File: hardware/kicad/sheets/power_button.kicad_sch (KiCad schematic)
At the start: 22 parts, among them J7 PANEL BUTTON, Q1 IRF4905S, Q2 BSS138, Q3 BSS138, Q4 BSS138, SW3 POWER, U11 LTC2954CTS8-2, U12 LM4040DBZ-5, U13 CL25N8-G

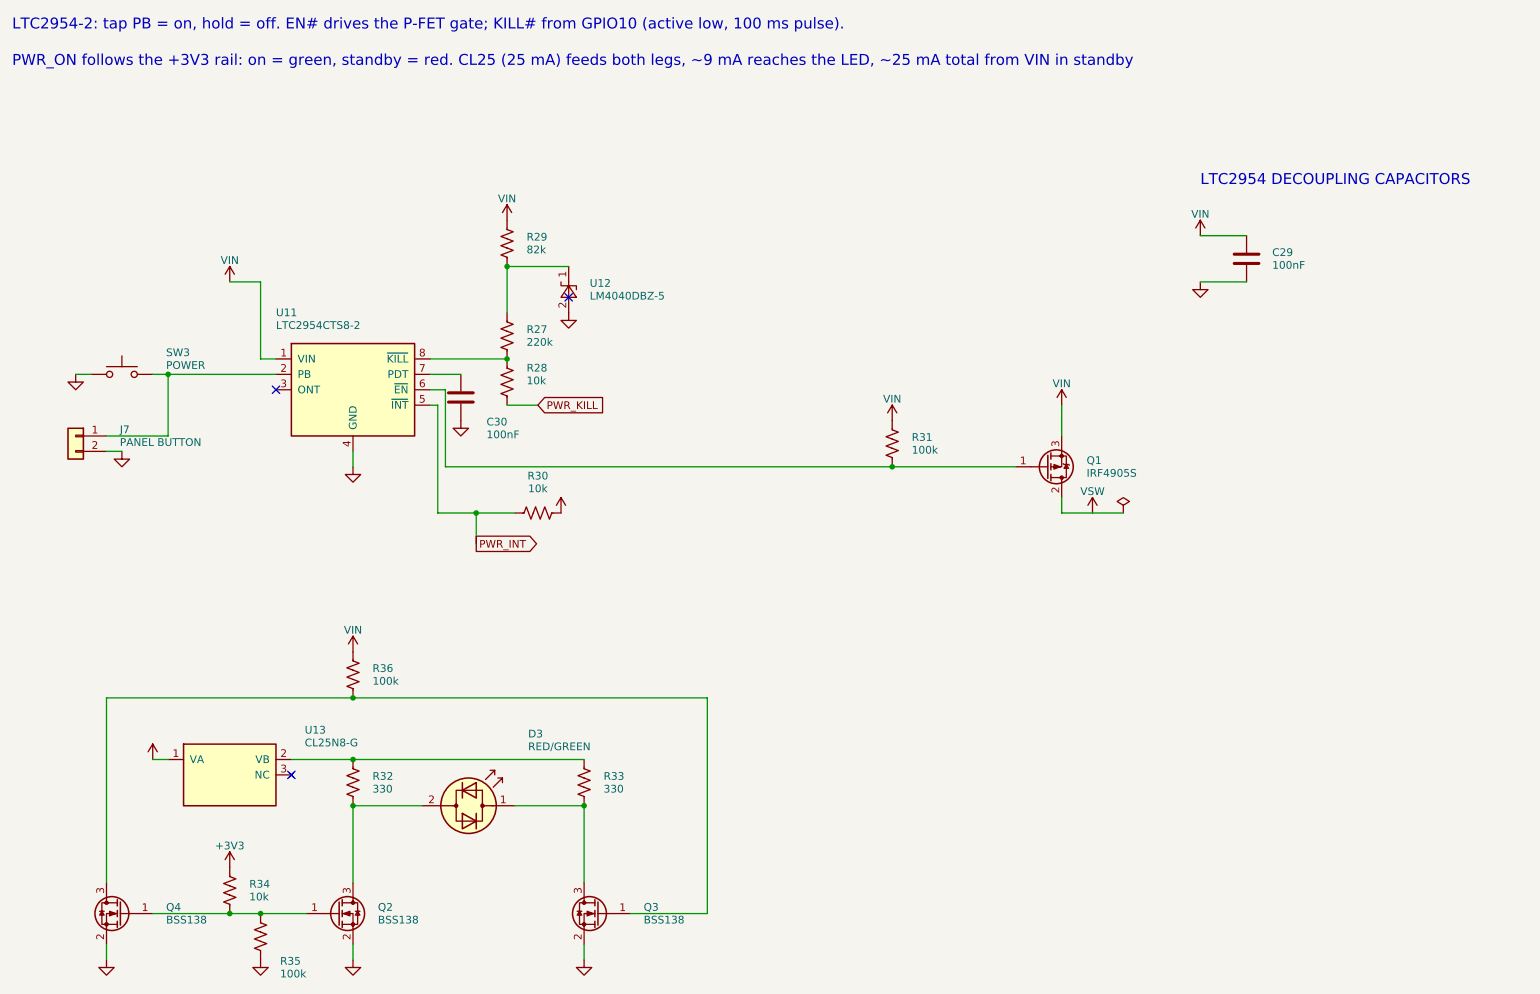
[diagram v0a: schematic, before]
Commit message: Put supply pins on top and grounds on the bottom of IC symbols; flake8-clean Python
Schematic: re-laid out pins on U2, U3, U6, U7, U11, U14, U17-U20, U22-U24
and PS1 (supply on top, ground/strap pins on the bottom edge) via custom
`cryocooler:` symbols (make_lib.from_stock) and a gnd_bus helper; U18/U2
use mirroring instead of a 180 degree rotation. Nets are unchanged (ERC 0,
117/117 datasheet rules, PCB nets still match). Text placement now shows
every power-symbol name, avoids wires, and uses a realistic character width.

Python: black -l 79 -S plus manual wrapping so hardware/kicad and scripts/
pass flake8; add .flake8.

Co-Authored-By: Claude Sonnet 5.5 <noreply@anthropic.com>
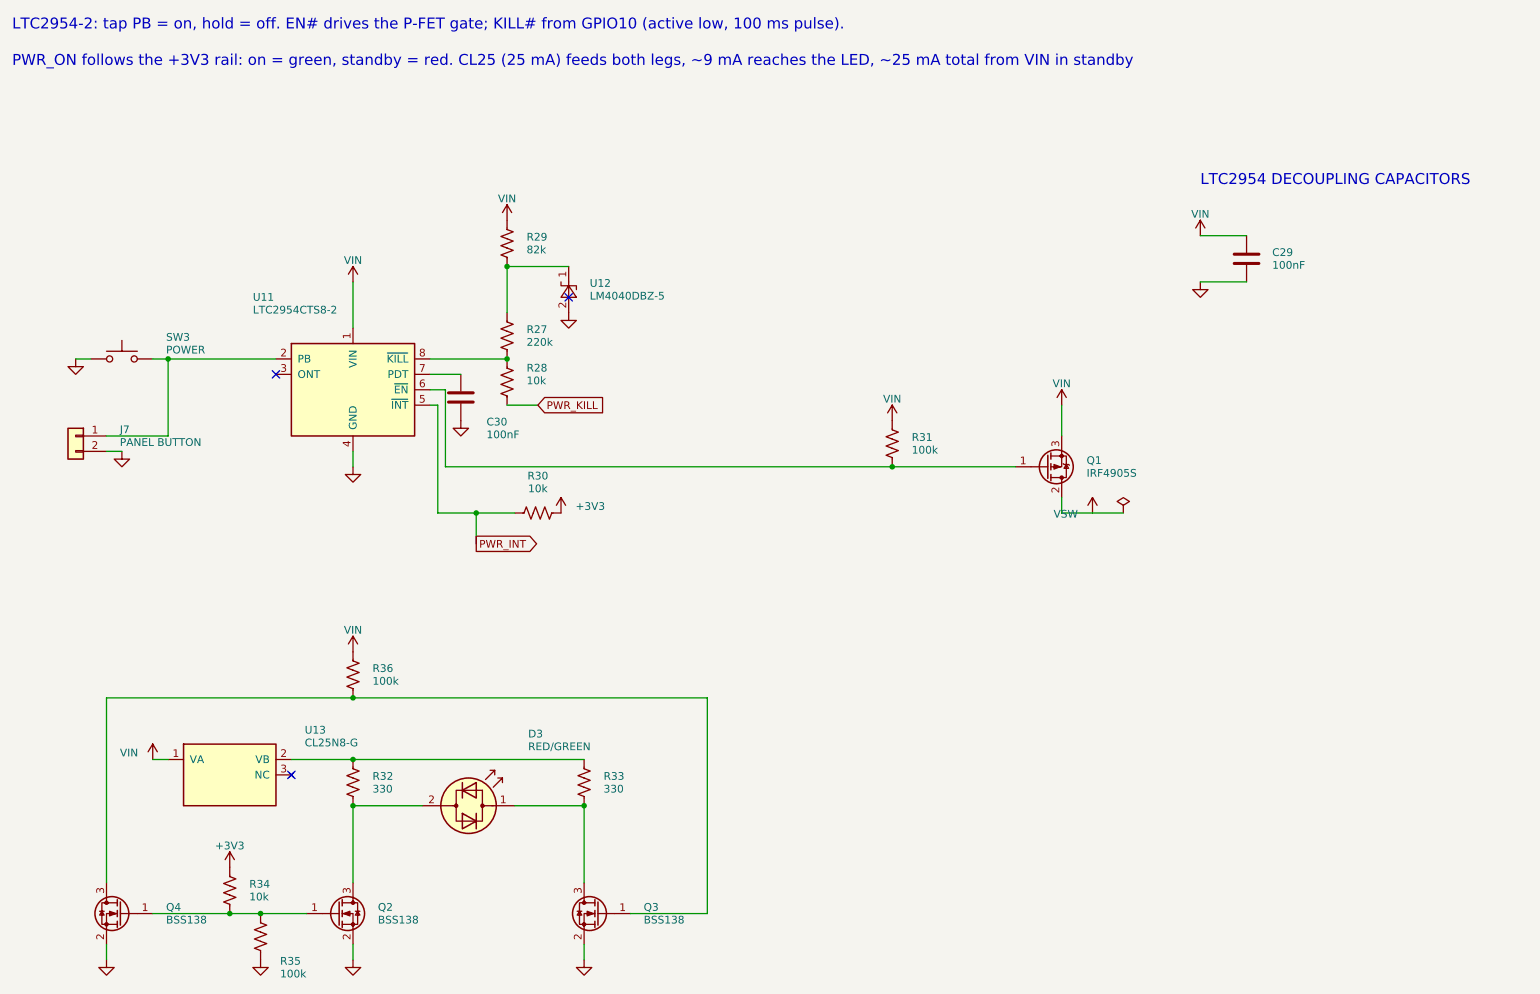
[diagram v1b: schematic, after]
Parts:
- removed D3: RED/GREEN, LED_SMD:LED_1206_3216Metric, symbol Device:LED_Dual_Bidirectional
- removed Q1: IRF4905S, Package_TO_SOT_SMD:TO-263-3_TabPin2, symbol Transistor_FET:IRF4905
- removed R36: 100k, Resistor_SMD:R_0603_1608Metric, symbol Device:R_US
- added C29: 100nF, Capacitor_SMD:C_0603_1608Metric, symbol Device:C
- added R33: 330, Resistor_SMD:R_0603_1608Metric, symbol Device:R_US
- added U13: CL25N8-G, Package_TO_SOT_SMD:SOT-89-3, symbol cryocooler:CL25N8-G
- C30: renamed from U12; value LM4040DBZ-5 -> 100nF; footprint Package_TO_SOT_SMD:SOT-23 -> Capacitor_SMD:C_0603_1608Metric; symbol Reference_Voltage:LM4040DBZ-5 -> Device:C
- D3: renamed from R32; value 330 -> RED/GREEN; footprint Resistor_SMD:R_0603_1608Metric -> LED_SMD:LED_1206_3216Metric; symbol Device:R_US -> Device:LED_Dual_Bidirectional
- J7: renamed from SW3; value POWER -> PANEL BUTTON; footprint Button_Switch_SMD:SW_SPST_TL3342 -> Connector_JST:JST_XH_B2B-XH-A_1x02_P2.50mm_Vertical; symbol Switch:SW_Push -> Connector_Generic:Conn_01x02
- Q1: renamed from R30; value 10k -> IRF4905S; footprint Resistor_SMD:R_0603_1608Metric -> Package_TO_SOT_SMD:TO-263-3_TabPin2; symbol Device:R_US -> Transistor_FET:IRF4905
- Q2: renamed from R33; value 330 -> BSS138; footprint Resistor_SMD:R_0603_1608Metric -> Package_TO_SOT_SMD:SOT-23; symbol Device:R_US -> Transistor_FET:BSS138
- R27: renamed from J7; value PANEL BUTTON -> 220k; footprint Connector_JST:JST_XH_B2B-XH-A_1x02_P2.50mm_Vertical -> Resistor_SMD:R_0603_1608Metric; symbol Connector_Generic:Conn_01x02 -> Device:R_US
- R29: renamed from R27; value 220k -> 82k
- R30: renamed from C30; value 100nF -> 10k; footprint Capacitor_SMD:C_0603_1608Metric -> Resistor_SMD:R_0603_1608Metric; symbol Device:C -> Device:R_US
- R32: renamed from U13; value CL25N8-G -> 330; footprint Package_TO_SOT_SMD:SOT-89-3 -> Resistor_SMD:R_0603_1608Metric; symbol cryocooler:CL25N8-G -> Device:R_US
- R34: renamed from Q4; value BSS138 -> 10k; footprint Package_TO_SOT_SMD:SOT-23 -> Resistor_SMD:R_0603_1608Metric; symbol Transistor_FET:BSS138 -> Device:R_US
- R35: renamed from R34; value 10k -> 100k
- SW3: renamed from C29; value 100nF -> POWER; footprint Capacitor_SMD:C_0603_1608Metric -> Button_Switch_SMD:SW_SPST_TL3342; symbol Device:C -> Switch:SW_Push
- U12: renamed from R29; value 82k -> LM4040DBZ-5; footprint Resistor_SMD:R_0603_1608Metric -> Package_TO_SOT_SMD:SOT-23; symbol Device:R_US -> Reference_Voltage:LM4040DBZ-5
- renumbered Q2 to Q3, Q3 to Q4, R35 to R36
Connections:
- net +3V3: now also R30.2, R34.1; no longer Q1.2, R35.1
- net GND: now also Q2.2 (S), R35.2, U12.2 (A), C29.2; no longer R27.2 (Pin_2), R30.2, R34.2 (S), R36.2
- net PWR_INT: now also R30.1; no longer Q1.1
- net VIN: now also Q1.3 (S), R29.1, R36.1, C29.1, U13.1 (VA); no longer R32.1 (VA), SW3.1, U12.1
- net VSW: now also Q1.2 (D)
- net at Q4.3 (D): now also Q3.1 (G), R36.2; no longer Q2.2
- net at D3.2 (AK): now also Q2.3 (D), R32.2; no longer Q3.3 (D)
- net at J7.1 (Pin_1), U11.2 (PB): now also SW3.1; no longer R27.1 (Pin_1)
- net at R31.2, U11.6 (~{EN}): now also Q1.1 (G)
- net at U11.7 (PDT): now also C30.1; no longer R30.1
- net at R28.1, U11.8 (~{KILL}): now also R27.2; no longer R29.2
- net at Q4.1 (G): now also Q2.1 (G), R34.2, R35.1; no longer R34.3 (D)
- new net: D3.1 (KA), Q3.3 (D), R33.2
- new net: R32.1, R33.1, U13.2 (VB)
- new net: R27.1, R29.2, U12.1 (K)
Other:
- moved on the sheet: Q3, Q4, R29, R35, R36, U12

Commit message: KiCad schematic: INA239, ADS1220, SC18IS604 bridge, relay driver, test points
- system_current: INA237 -> INA239 (SPI, CS GPIO3) with the 49.9 ohm / 470 nF
  input filter, power LED and ALERT LED; VBUS shares the filtered IN- node.
- cold_head: ADS122C04 -> ADS1220 (SPI, CS GPIO44).
- i2c_bridge (new): SC18IS604 SPI-to-I2C bridge for the EMC2303, with a
  74LVC1G125 gating its MISO onto the shared bus.
- compressor_relay (new): GPIO16 high-side switch sharing one generator
  function with the amplifier REM switch.
- debug (new): about 40 test points and rail LEDs (the isolated rail LED
  returns to ISO_GND).
- ISO7741 -> ACS37800 SPI lines are straight wires (pins reordered on the
  symbol); USB_VBUS is one wire plus a naming label.
- Custom symbols for INA239, ADS1220, SC18IS604; datasheet rules 117 -> 162;
  GPIO map checks updated. ERC 0.

Co-Authored-By: Claude Sonnet 5.5 <noreply@anthropic.com>
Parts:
- removed Q2, Q3: BSS138, Package_TO_SOT_SMD:SOT-23, symbol Transistor_FET:BSS138
- removed R28: 10k, Resistor_SMD:R_0603_1608Metric, symbol Device:R_US
- removed R31, R35, R36: 100k, Resistor_SMD:R_0603_1608Metric, symbol Device:R_US
- added D3: RED/GREEN, LED_SMD:LED_1206_3216Metric, symbol Device:LED_Dual_Bidirectional
- added R26, R32: 10k, Resistor_SMD:R_0603_1608Metric, symbol Device:R_US
- added R30: 330, Resistor_SMD:R_0603_1608Metric, symbol Device:R_US
- added SW3: POWER, Button_Switch_SMD:SW_SPST_TL3342, symbol Switch:SW_Push
- added U11: LTC2954CTS8-2, Package_TO_SOT_SMD:SOT-23-8, symbol cryocooler:LTC2954CTS8-2
- added U13: CL25N8-G, Package_TO_SOT_SMD:SOT-89-3, symbol cryocooler:CL25N8-G
- C29: renamed from U11; value LTC2954CTS8-2 -> 100nF; footprint Package_TO_SOT_SMD:SOT-23-8 -> Capacitor_SMD:C_0603_1608Metric; symbol cryocooler:LTC2954CTS8-2 -> Device:C
- C30: renamed from R29; value 82k -> 100nF; footprint Resistor_SMD:R_0603_1608Metric -> Capacitor_SMD:C_0603_1608Metric; symbol Device:R_US -> Device:C
- J7: renamed from C29; value 100nF -> PANEL BUTTON; footprint Capacitor_SMD:C_0603_1608Metric -> Connector_JST:JST_XH_B2B-XH-A_1x02_P2.50mm_Vertical; symbol Device:C -> Connector_Generic:Conn_01x02
- Q2: renamed from R32; value 330 -> BSS138; footprint Resistor_SMD:R_0603_1608Metric -> Package_TO_SOT_SMD:SOT-23; symbol Device:R_US -> Transistor_FET:BSS138
- Q3: renamed from D3; value RED/GREEN -> BSS138; footprint LED_SMD:LED_1206_3216Metric -> Package_TO_SOT_SMD:SOT-23; symbol Device:LED_Dual_Bidirectional -> Transistor_FET:BSS138
- R25: renamed from SW3; value POWER -> 220k; footprint Button_Switch_SMD:SW_SPST_TL3342 -> Resistor_SMD:R_0603_1608Metric; symbol Switch:SW_Push -> Device:R_US
- R27: renamed from J7; value PANEL BUTTON -> 82k; footprint Connector_JST:JST_XH_B2B-XH-A_1x02_P2.50mm_Vertical -> Resistor_SMD:R_0603_1608Metric; symbol Connector_Generic:Conn_01x02 -> Device:R_US
- R28: renamed from U12; value LM4040DBZ-5 -> 10k; footprint Package_TO_SOT_SMD:SOT-23 -> Resistor_SMD:R_0603_1608Metric; symbol Reference_Voltage:LM4040DBZ-5 -> Device:R_US
- R29: renamed from R30; value 10k -> 100k
- R31: renamed from U13; value CL25N8-G -> 330; footprint Package_TO_SOT_SMD:SOT-89-3 -> Resistor_SMD:R_0603_1608Metric; symbol cryocooler:CL25N8-G -> Device:R_US
- R33: value 330 -> 100k
- R34: value 10k -> 100k
- TP1: renamed from C30; value 100nF -> LTC2954_INT; footprint Capacitor_SMD:C_0603_1608Metric -> TestPoint:TestPoint_Pad_D1.5mm; symbol Device:C -> Connector:TestPoint
- U12: renamed from R27; value 220k -> LM4040DBZ-5; footprint Resistor_SMD:R_0603_1608Metric -> Package_TO_SOT_SMD:SOT-23; symbol Device:R_US -> Reference_Voltage:LM4040DBZ-5
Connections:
- net +3V3: now also R28.2, R32.1; no longer R29.2, R34.1
- net GND: now also C29.2, C30.2, Q2.2 (S), Q3.2 (S), R33.2, U12.2 (A), SW3.2, U11.4 (GND); no longer C29.4 (GND), R25.2, R27.2 (Pin_2), R28.2 (A), TP1.2
- net PWR_KILL: now also R26.2
- net VIN: now also R27.1, R29.1, R34.1, U11.1 (VIN), U13.1 (VA); no longer C30.1, J7.1, R31.1 (VA)
- net at Q4.1 (G): now also Q2.1 (G), R33.1, R32.2; no longer R34.2
- net at Q4.3 (D): now also Q3.1 (G), R34.2
- net at TP1.1: now also R28.1, U11.5 (~{INT}); no longer C29.7 (PDT)
- net at Q1.1 (G): now also R29.2, U11.6 (~{EN}); no longer C29.6 (~{EN})
- removed net PWR_INT: C29.5 (~{INT}), R29.1
- new net: J7.1 (Pin_1), SW3.1, U11.2 (PB)
- new net: C30.1, U11.7 (PDT)
- new net: R25.2, R26.1, U11.8 (~{KILL})
- new net: R25.1, R27.2, U12.1 (K)
- new net: R30.1, R31.1, U13.2 (VB)
- new net: D3.2 (AK), Q2.3 (D), R30.2
- new net: D3.1 (KA), Q3.3 (D), R31.2
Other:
- moved on the sheet: R28, R29, U12
